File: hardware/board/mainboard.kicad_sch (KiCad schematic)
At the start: 0 parts

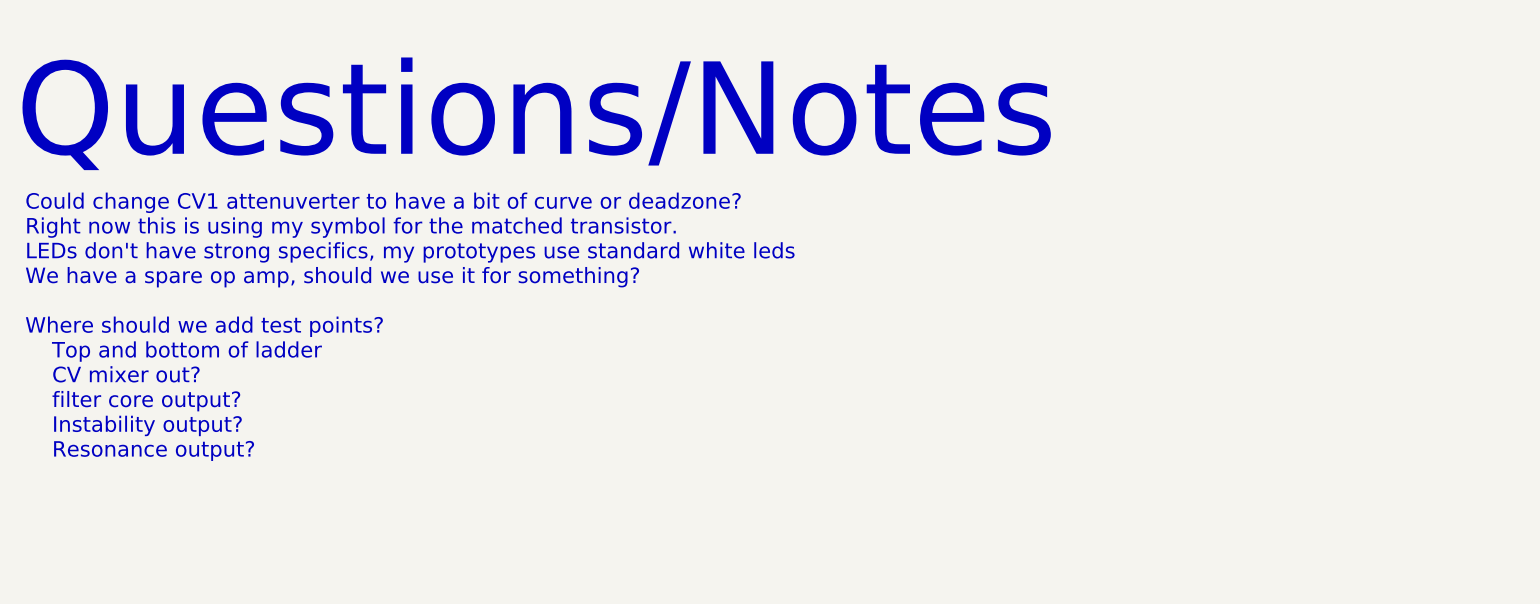
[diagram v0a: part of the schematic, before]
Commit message: Schematic getting closer to being finished
Schematic should be close to being ready to assign MPNs.
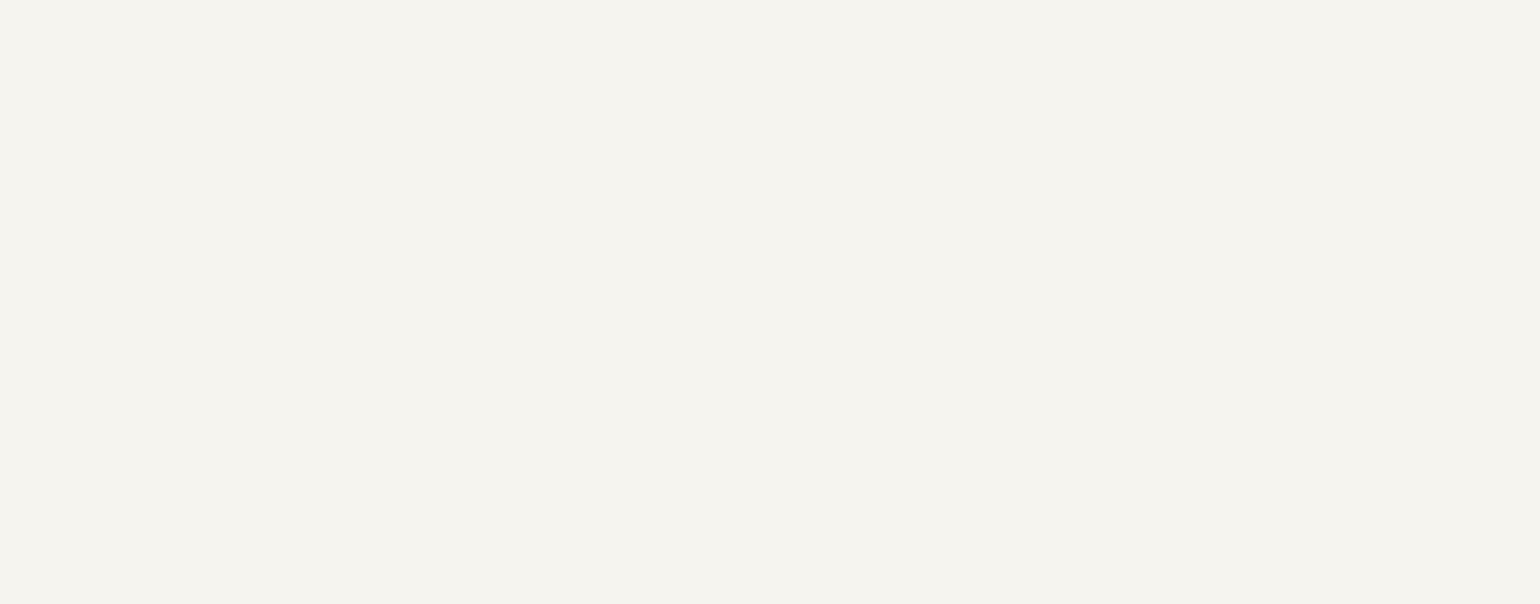
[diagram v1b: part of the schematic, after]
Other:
- note removed: "Could change CV1 attenuverter to have a bit of curve or deadzone? Right now this is using my symbol for the matched transistor. LEDs don't have strong specifics, my prototypes use standard white leds We have a spare op amp, should we use it for something? Where should we add test points? Top and bottom of ladder CV mixer out? filter core output? Instability output? Resonance output?"
- note removed: "Questions/Notes"
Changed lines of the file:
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@@
     (stroke (width 0) (type default))
-  )
-  (text "Could change CV1 attenuverter to have a bit of curve or deadzone?\nRight now this is using my symbol for the matched transistor.\nLEDs don't have strong specifics, my prototypes use standard white leds\nWe have a spare op amp, should we use it for something?\n\nWhere should we add test points?\n	Top and bottom of ladder\n	CV mixer out?\n	filter core output?\n	Instability output?\n	Resonance output?\n"
-    (at 0 -2.54 0)
-    (effects (font (size 2 2)) (justify left bottom))
   )
   (text "Diode Ladder Filter" (at 17.78 25.4 0)
     (effects (font (size 5 5) (thickness 0.508) bold) (justify left bottom))
   )
-  (text "Questions/Notes" (at -1.27 -40.64 0)
-    (effects (font (size 12 12)) (justify left bottom))
-  )
   (text "4 Pole Diode Ladder Filter\n\nInspired by the filter by Moritz Klein\n\n\n"

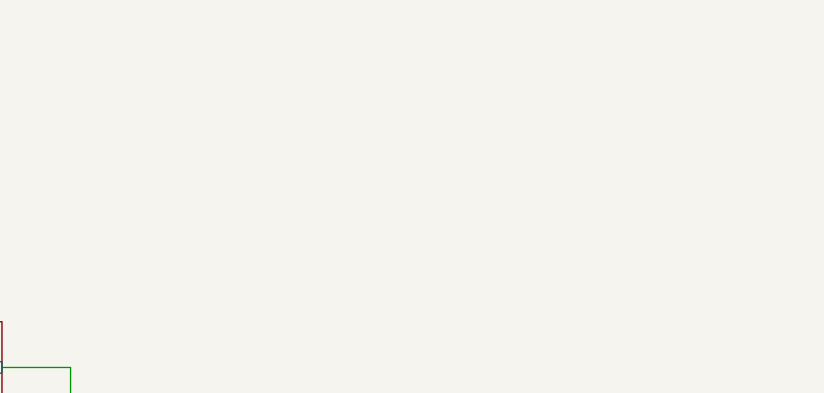
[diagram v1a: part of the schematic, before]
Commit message: BOM Consolidation
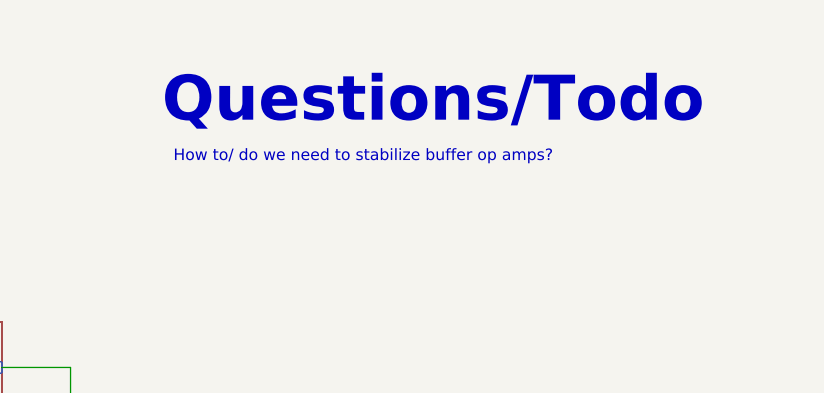
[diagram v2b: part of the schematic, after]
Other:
- note added: "How to/ do we need to stabilize buffer op amps?"
- note added: "Questions/Todo"
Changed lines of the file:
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@@
     (stroke (width 0) (type default))
+  )
+  (text "Questions/Todo" (at 194.31 29.21 0)
+    (effects (font (size 5 5) (thickness 0.508) bold) (justify left bottom))
   )
   (text "Diode Ladder Filter" (at 17.78 25.4 0)
     (effects (font (size 5 5) (thickness 0.508) bold) (justify left bottom))
   )
+  (text "How to/ do we need to stabilize buffer op amps?\n\n\n\n"
+    (at 195.58 39.37 0)
+    (effects (font (size 1.27 1.27)) (justify left bottom))
+  )
   (text "4 Pole Diode Ladder Filter\n\nInspired by the filter by Moritz Klein\n\n\n"

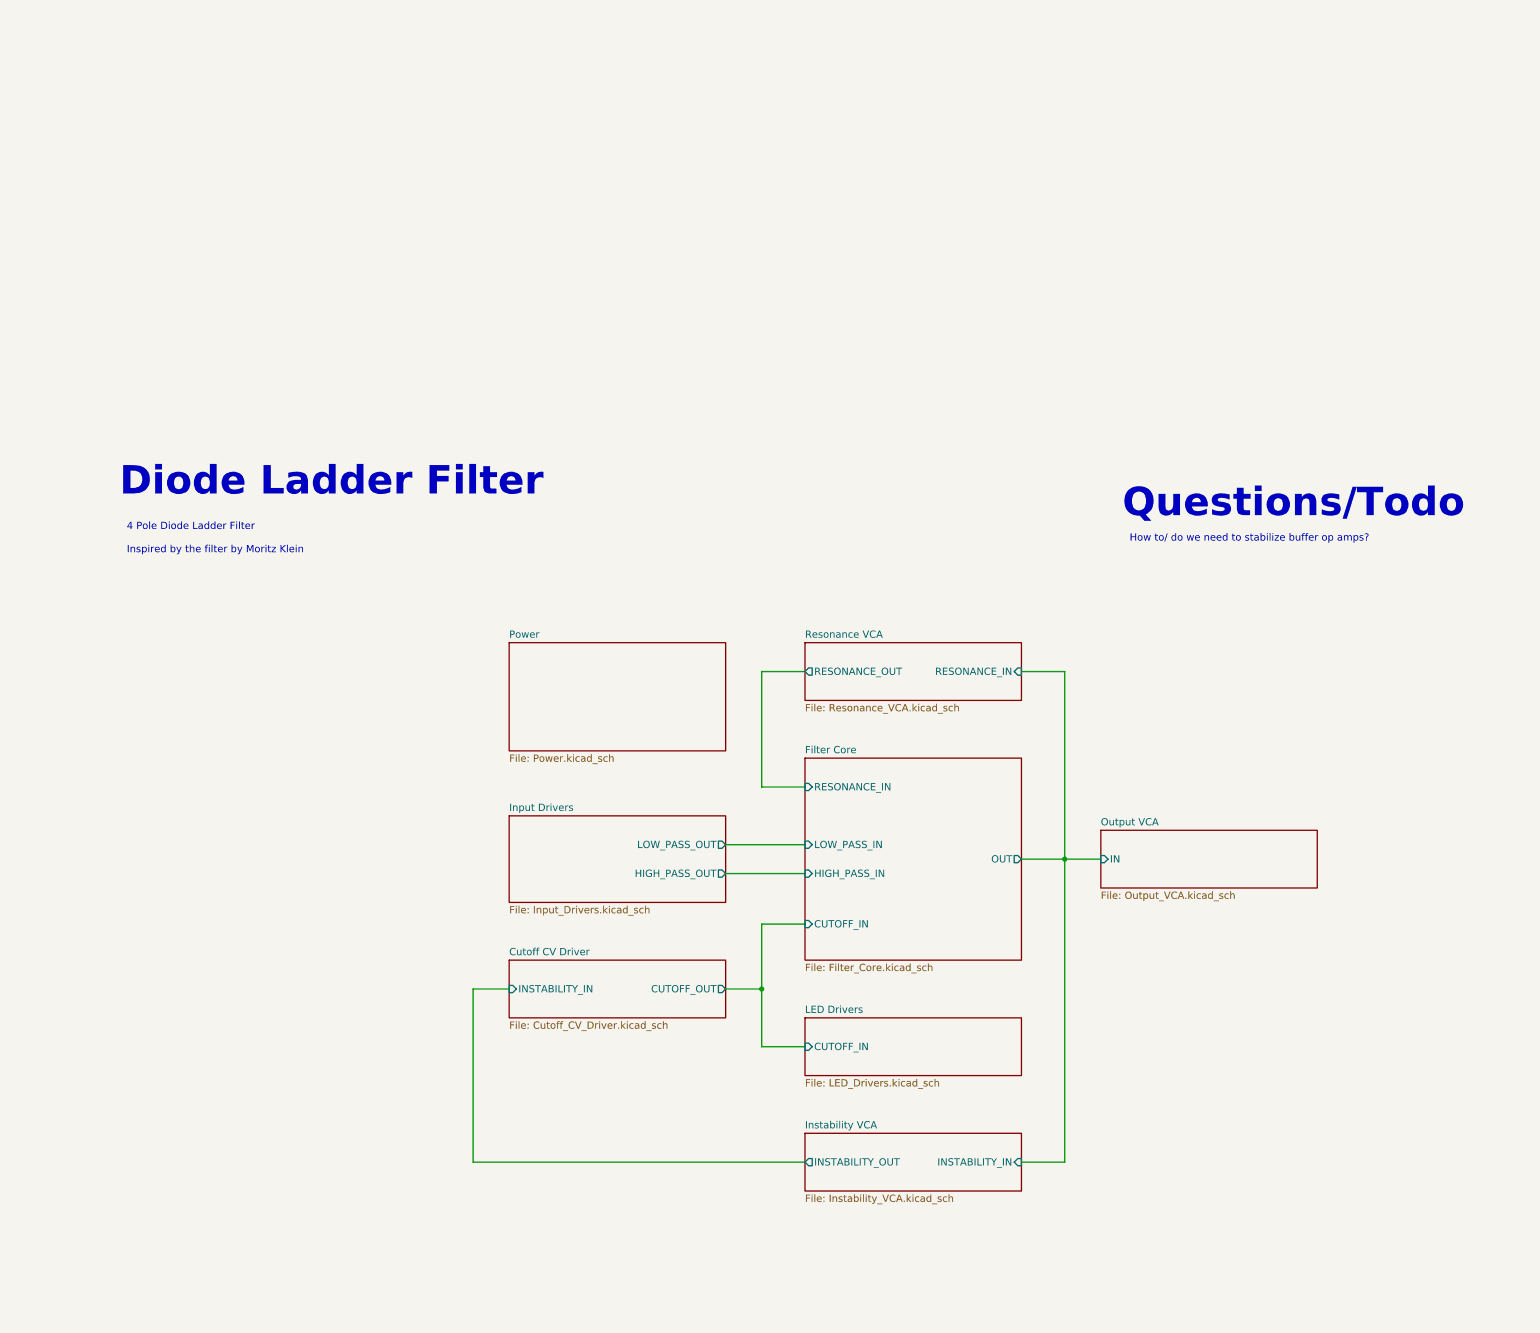
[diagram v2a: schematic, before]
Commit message: Updates for LED Drivers
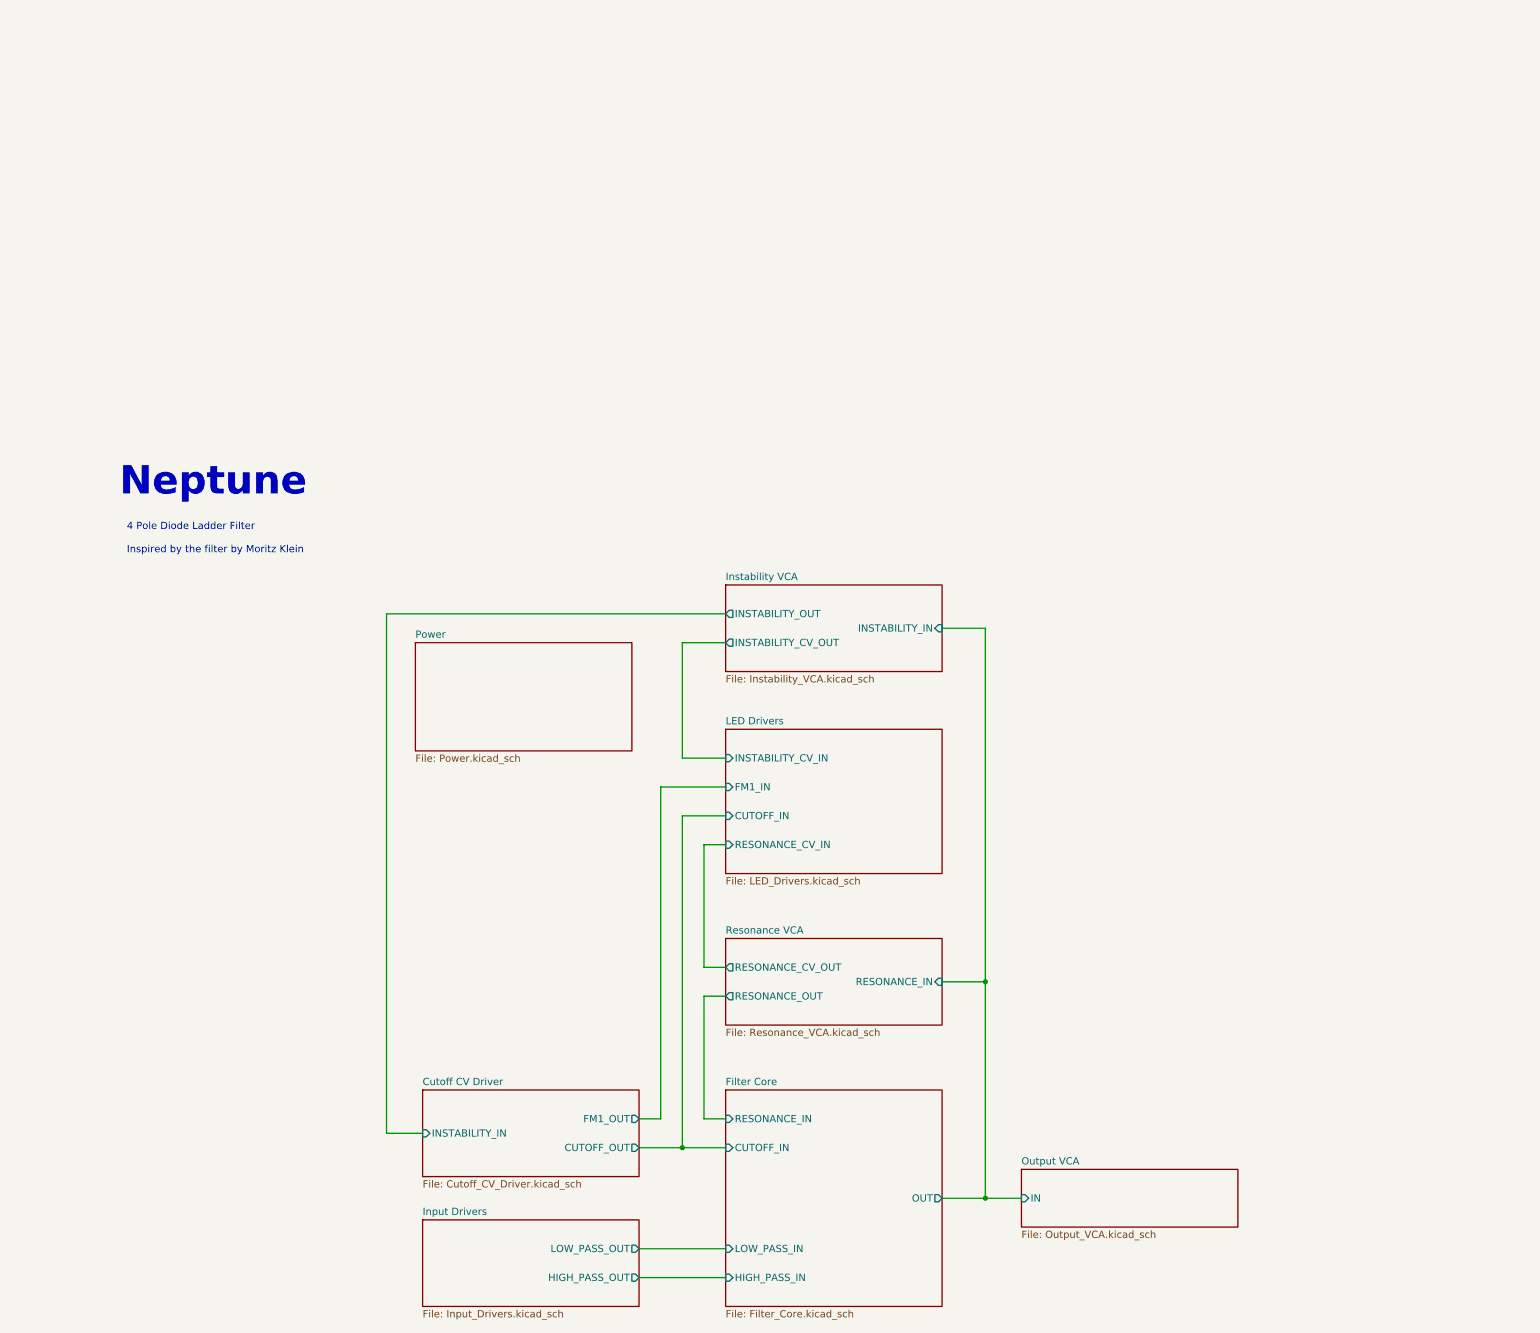
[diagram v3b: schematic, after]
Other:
- sheet Cutoff CV Driver ports: added FM1_OUT; removed none
- sheet Instability VCA ports: added INSTABILITY_CV_OUT; removed none
- sheet LED Drivers ports: added FM1_IN, INSTABILITY_CV_IN, RESONANCE_CV_IN; removed none
- sheet Resonance VCA ports: added RESONANCE_CV_OUT; removed none
- note added: "Neptune"
- note removed: "Diode Ladder Filter"
- note removed: "How to/ do we need to stabilize buffer op amps?"
- note removed: "Questions/Todo"
